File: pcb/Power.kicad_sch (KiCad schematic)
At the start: 32 parts, among them J2 Barrel_Jack, Q1 DMP3013SFV-7, U4 AP64501SP-13

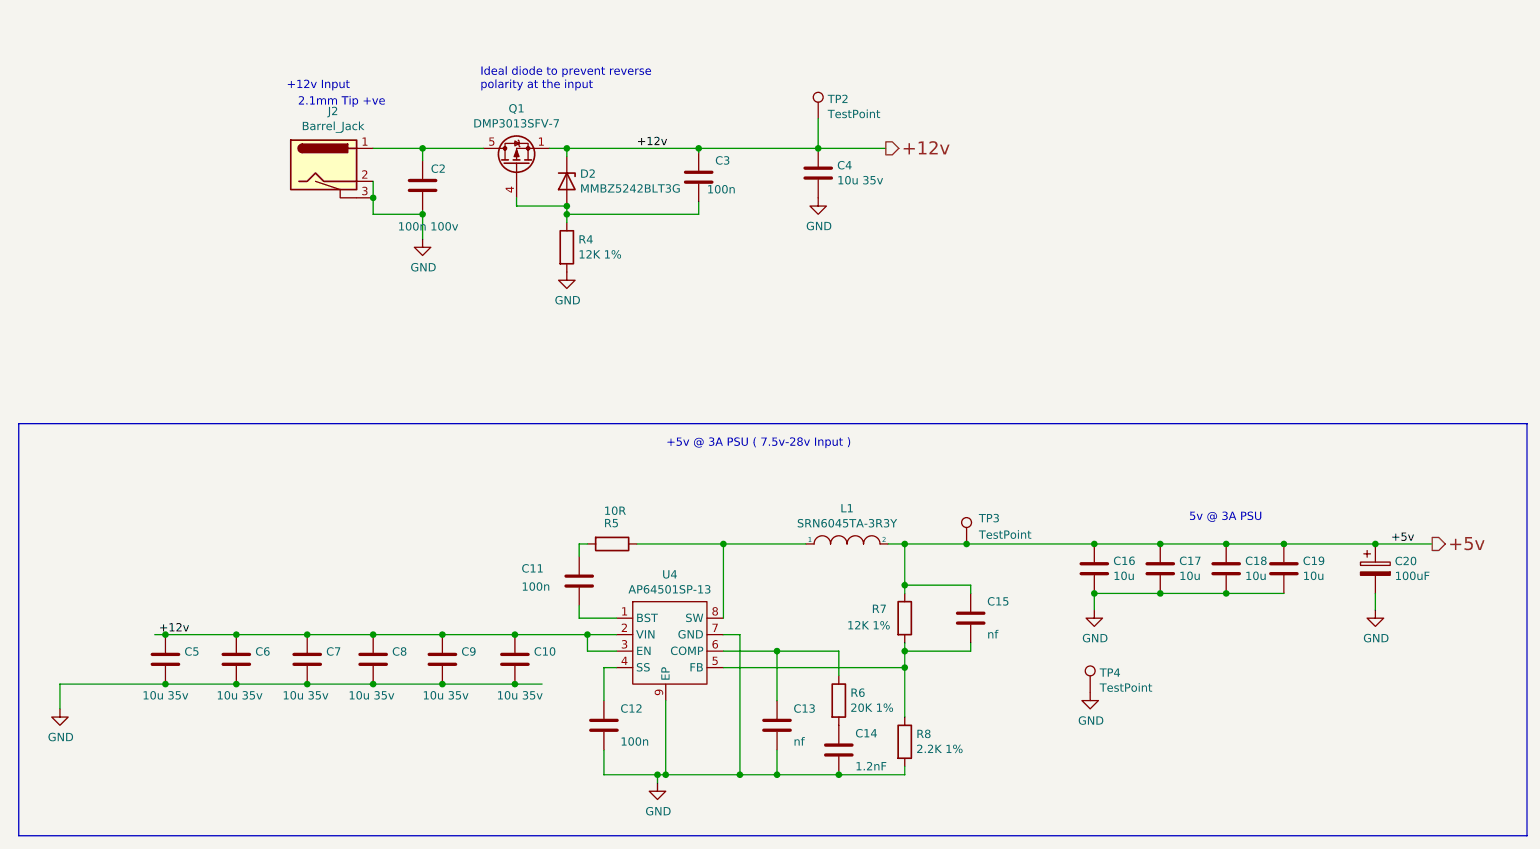
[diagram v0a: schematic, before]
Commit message: - USB sound wired
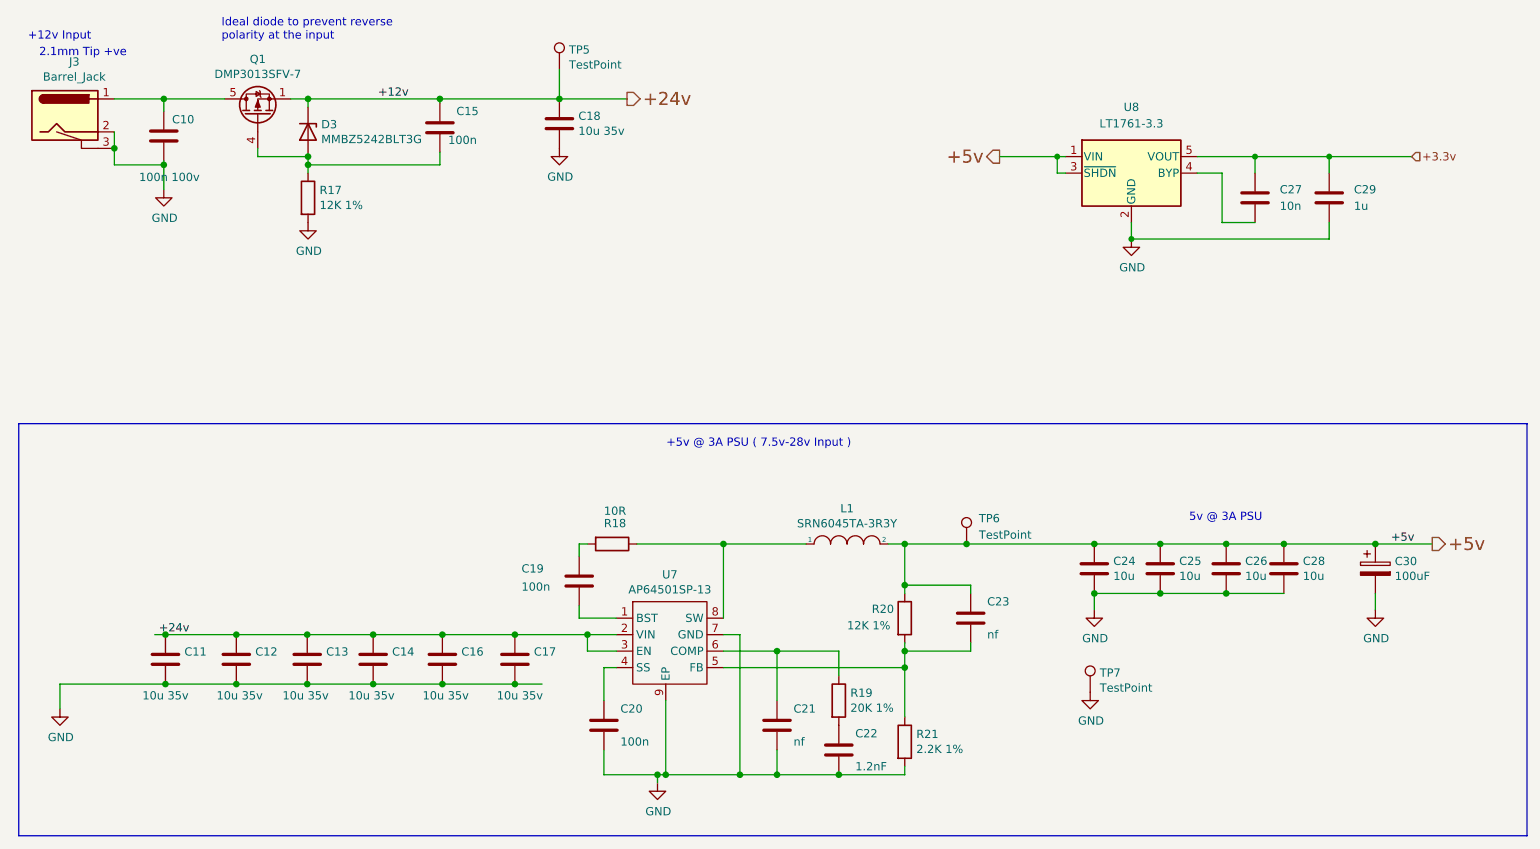
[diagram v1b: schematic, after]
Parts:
- added C27: 10n, symbol Device:C
- added C29: 1u, symbol Device:C
- added U8: LT1761-3.3, Package_TO_SOT_SMD:TSOT-23-5, symbol Regulator_Linear:LT1761-3.3
- renumbered C2 to C10, C5 to C11, C6 to C12, C7 to C13, C8 to C14, C3 to C15, C9 to C16, C10 to C17, C4 to C18, C11 to C19, C12 to C20, C13 to C21, C14 to C22, C15 to C23, C16 to C24, C17 to C25, C18 to C26, C19 to C28, C20 to C30, D2 to D3, J2 to J3, R4 to R17, R5 to R18, R6 to R19, R7 to R20, R8 to R21, TP2 to TP5, TP3 to TP6, TP4 to TP7, U4 to U7
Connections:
- net +5v: now also U8.1 (VIN), U8.3 (~{SHDN})
- net GND: now also C29.2, U8.2 (GND)
- net +12v renamed +24v
- new net: C27.2, U8.4 (BYP)
- new net +3.3v: C27.1, C29.1, U8.5 (VOUT)
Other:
- moved on the sheet: C10, C15, C18, D3, J3, Q1, R17, TP5

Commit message: - work in progress
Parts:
- renumbered TP5 to TP7, TP6 to TP8, TP7 to TP9

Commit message: - voor aanpassing design rules jclpcb
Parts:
- removed J3: Barrel_Jack, CM4IO:BarrelJack_Horizontal, symbol CM4IO:Barrel_Jack
- added J5: 24v Input, TerminalBlock:TerminalBlock_bornier-2_P5.08mm, symbol Connector:Screw_Terminal_01x02
- C10, C15, C19, C20, C21, C22, C23: footprint Capacitor_SMD:C_0402_1005Metric -> Capacitor_SMD:C_0805_2012Metric_Pad1.18x1.45mm_HandSolder
- C11, C12, C13, C14, C16, C17, C18, C24, C25, C26, C28: footprint Capacitor_SMD:C_0805_2012Metric -> Capacitor_SMD:C_0805_2012Metric_Pad1.18x1.45mm_HandSolder
- C27, C29: footprint (none) -> Capacitor_SMD:C_0805_2012Metric_Pad1.18x1.45mm_HandSolder
- R17, R18, R19, R20, R21: footprint Resistor_SMD:R_0402_1005Metric -> Resistor_SMD:R_0805_2012Metric_Pad1.20x1.40mm_HandSolder
- TP7, TP8, TP9: footprint TestPoint:TestPoint_Pad_2.0x2.0mm -> TestPoint:TestPoint_Bridge_Pitch2.54mm_Drill1.0mm
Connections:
- net GND: now also J5.1 (Pin_1)
- net at C10.1, Q1.5 (D): now also J5.2 (Pin_2)
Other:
- note removed: "+12v Input"
- note removed: "2.1mm Tip +ve"

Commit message: - amp connected
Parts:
- renumbered J5 to J3, TP7 to TP10, TP8 to TP11, TP9 to TP12
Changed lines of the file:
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@@
   (symbol (lib_id "Connector:Screw_Terminal_01x02") (at 34.29 45.72 180) (unit 1)
     (in_bom yes) (on_board yes) (dnp no) (fields_autoplaced)
-    (property "Reference" "J5" (at 34.29 36.83 0)
+    (property "Reference" "J3" (at 34.29 36.83 0)
       (effects (font (size 1.27 1.27)))
     )
@@
       (project "VolumioAmp"
         (path "/c639bae0-d26f-43ee-9e8c-ca060284bd0b/97b9f385-290b-4a5e-9fd5-e8b1b07223d1"
-          (reference "J5") (unit 1)
+          (reference "J3") (unit 1)
         )
       )
@@
   (symbol (lib_id "Connector:TestPoint") (at 172.72 111.76 0) (unit 1)
     (in_bom yes) (on_board yes) (dnp no)
-    (property "Reference" "TP8" (at 174.625 107.823 0)
+    (property "Reference" "TP11" (at 174.625 107.823 0)
       (effects (font (size 1.27 1.27)) (justify left))
     )
@@
       (project "VolumioAmp"
         (path "/c639bae0-d26f-43ee-9e8c-ca060284bd0b/97b9f385-290b-4a5e-9fd5-e8b1b07223d1"
-          (reference "TP8") (unit 1)
+          (reference "TP11") (unit 1)
         )
       )
@@
   (symbol (lib_id "Connector:TestPoint") (at 109.982 38.608 0) (unit 1)
     (in_bom yes) (on_board yes) (dnp no)
-    (property "Reference" "TP7" (at 111.4552 35.6108 0)
+    (property "Reference" "TP10" (at 111.4552 35.6108 0)
       (effects (font (size 1.27 1.27)) (justify left))
     )
@@
       (project "VolumioAmp"
         (path "/c639bae0-d26f-43ee-9e8c-ca060284bd0b/97b9f385-290b-4a5e-9fd5-e8b1b07223d1"
-          (reference "TP7") (unit 1)
+          (reference "TP10") (unit 1)
         )
       )
@@
   (symbol (lib_id "Connector:TestPoint") (at 191.77 134.62 0) (unit 1)
     (in_bom yes) (on_board yes) (dnp no)
-    (property "Reference" "TP9" (at 193.2432 131.6228 0)
+    (property "Reference" "TP12" (at 193.2432 131.6228 0)
       (effects (font (size 1.27 1.27)) (justify left))
     )
@@
       (project "VolumioAmp"
         (path "/c639bae0-d26f-43ee-9e8c-ca060284bd0b/97b9f385-290b-4a5e-9fd5-e8b1b07223d1"
-          (reference "TP9") (unit 1)
-        )
-      )
+          (reference "TP12") (unit 1)
+        )
+      )

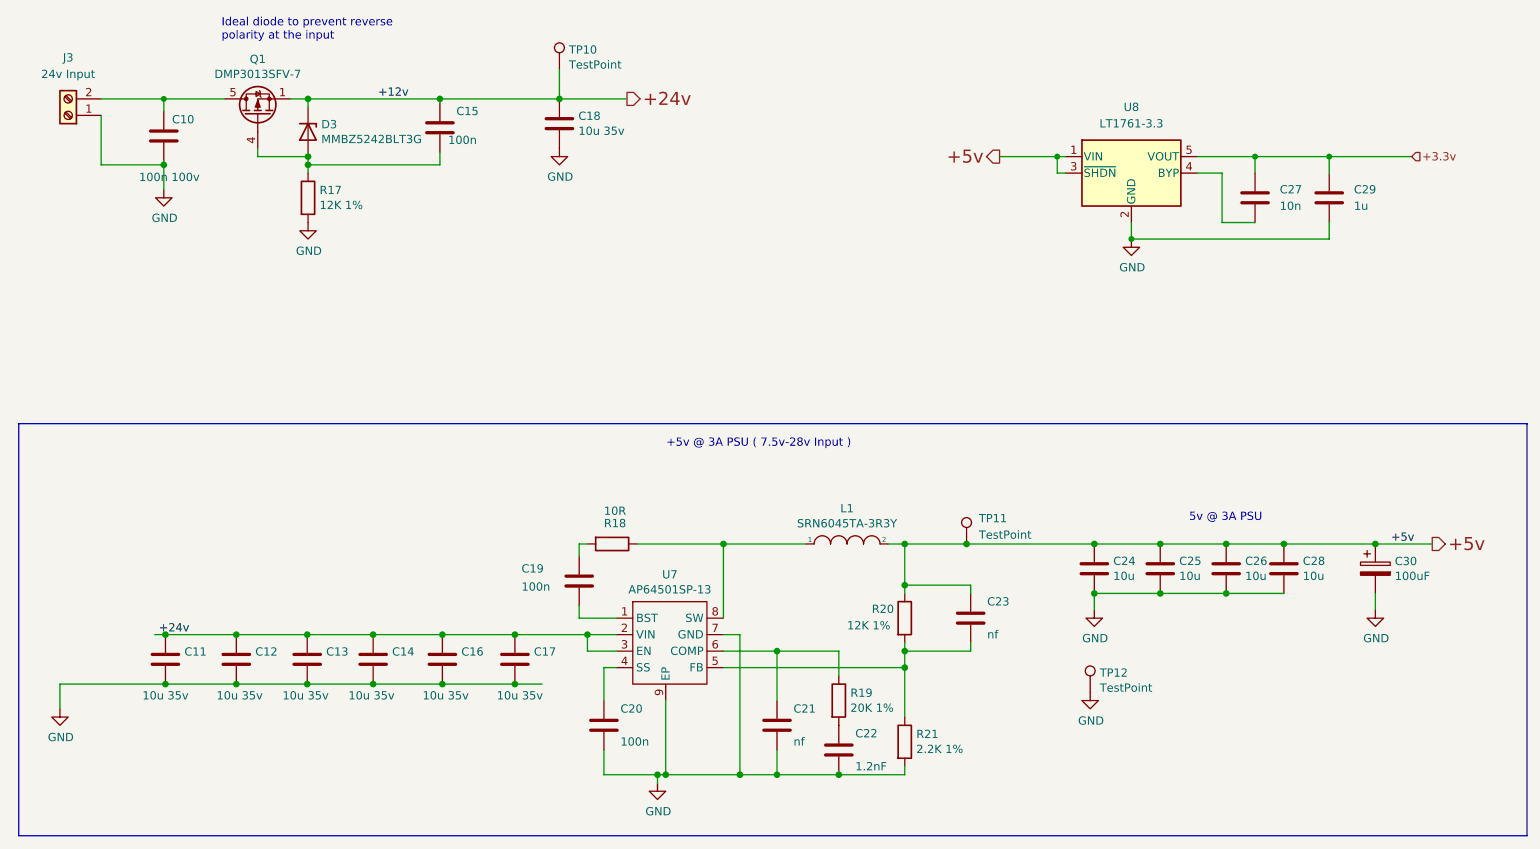
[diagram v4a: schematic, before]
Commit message: - cleanup ERC errors
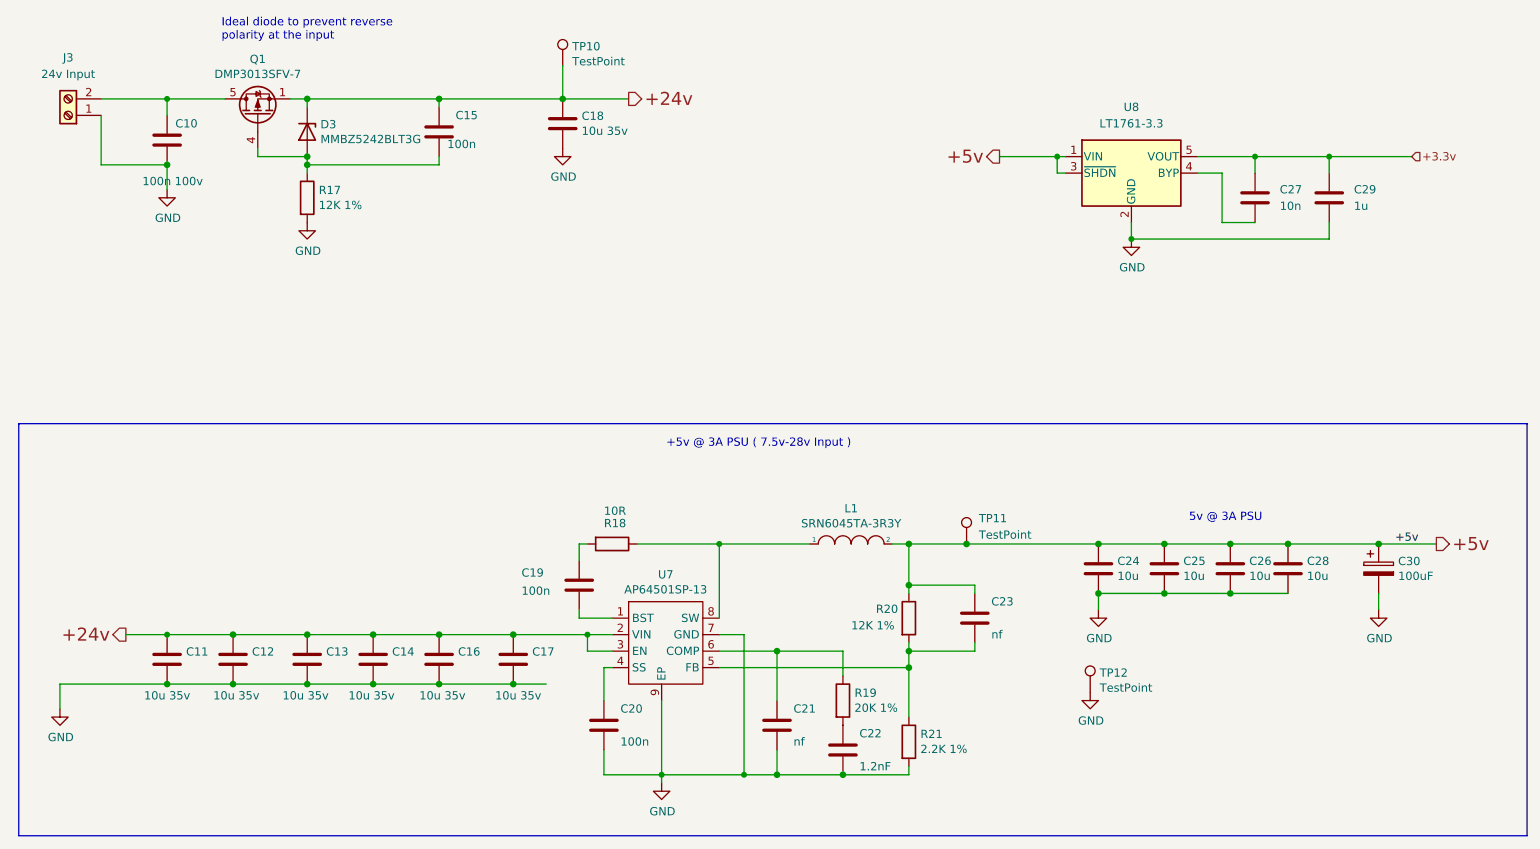
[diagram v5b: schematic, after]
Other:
- moved on the sheet: C10, C12, C15, C16, C18, C19, C22, C23, C24, C25, C26, C28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

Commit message: - ERC checks
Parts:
- D3: footprint Diode_SMD:D_SOT-23_ANK -> Package_TO_SOT_SMD:SOT-23
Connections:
- net +24v: now also D3.3 (K); no longer D3.1 (K)
- net at C15.2, Q1.4 (G), R17.1: now also D3.1 (A); no longer D3.2 (A)
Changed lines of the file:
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@@
     (effects (font (size 2.0066 2.0066)) (justify right))
   )
-  (symbol (lib_id "power:GND") (at 49.53 57.15 0) (unit 1)
+  (symbol (lib_name "GND_2") (lib_id "power:GND") (at 49.53 57.15 0) (unit 1)
     (in_bom yes) (on_board yes) (dnp no)
     (property "Reference" "#PWR021" (at 49.53 63.5 0)
@@
     )
   )
-  (symbol (lib_id "power:GND") (at 236.22 121.92 0) (unit 1)
+  (symbol (lib_name "GND_5") (lib_id "power:GND") (at 236.22 121.92 0) (unit 1)
     (in_bom yes) (on_board yes) (dnp no)
     (property "Reference" "#PWR028" (at 236.22 128.27 0)
@@
     )
   )
-  (symbol (lib_id "power:GND") (at 110.49 50.8 0) (unit 1)
+  (symbol (lib_name "GND_3") (lib_id "power:GND") (at 110.49 50.8 0) (unit 1)
     (in_bom yes) (on_board yes) (dnp no)
     (property "Reference" "#PWR023" (at 110.49 57.15 0)
@@
       (effects (font (size 1.27 1.27)) (justify left))
     )
-    (property "Footprint" "Diode_SMD:D_SOT-23_ANK" (at 66.675 48.26 0)
+    (property "Footprint" "Package_TO_SOT_SMD:SOT-23" (at 66.675 48.26 0)
       (effects (font (size 1.27 1.27)) hide)
     )
@@
     (pin "1")
     (pin "2")
+    (pin "3")
     (instances
       (project "VolumioAmp"
@@
     )
   )
-  (symbol (lib_id "power:GND") (at 71.12 62.23 0) (unit 1)
+  (symbol (lib_name "GND_1") (lib_id "power:GND") (at 71.12 62.23 0) (unit 1)
     (in_bom yes) (on_board yes) (dnp no)
     (property "Reference" "#PWR022" (at 71.12 68.58 0)
@@
     )
   )
-  (symbol (lib_id "power:GND") (at 125.73 148.59 0) (unit 1)
+  (symbol (lib_name "GND_7") (lib_id "power:GND") (at 125.73 148.59 0) (unit 1)
     (in_bom yes) (on_board yes) (dnp no)
     (property "Reference" "#PWR024" (at 125.73 154.94 0)
@@
     )
   )
-  (symbol (lib_id "power:GND") (at 191.77 134.62 0) (unit 1)
+  (symbol (lib_name "GND_8") (lib_id "power:GND") (at 191.77 134.62 0) (unit 1)
     (in_bom yes) (on_board yes) (dnp no)
     (property "Reference" "#PWR025" (at 191.77 140.97 0)
@@
     )
   )
-  (symbol (lib_id "power:GND") (at 193.04 121.92 0) (unit 1)
+  (symbol (lib_name "GND_4") (lib_id "power:GND") (at 193.04 121.92 0) (unit 1)
     (in_bom yes) (on_board yes) (dnp no)
     (property "Reference" "#PWR026" (at 193.04 128.27 0)
@@
     )
   )
-  (symbol (lib_id "power:GND") (at 33.02 137.16 0) (unit 1)
+  (symbol (lib_name "GND_6") (lib_id "power:GND") (at 33.02 137.16 0) (unit 1)
     (in_bom yes) (on_board yes) (dnp no)
     (property "Reference" "#PWR020" (at 33.02 143.51 0)
